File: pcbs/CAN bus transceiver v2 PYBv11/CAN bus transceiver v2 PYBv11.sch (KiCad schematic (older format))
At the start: 5 parts, among them P1 CONN_01X16, P2 CONN_01X02, P3 CONN_01X16, U1 TCAN337GDR, U2 TCAN337GDR

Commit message: working on CAN bus transceiver v2 PYBv11 shield
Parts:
- removed P1, P3: CONN_01X16, Pin_Headers:Pin_Header_Straight_1x16, symbol CONN_01X16
- added P1, P3: CONN_01X06, Pin_Headers:Pin_Header_Straight_1x06, symbol CONN_01X06
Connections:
- net +3V3: now also P3.2 (P2)
- net GND: now also P3.3 (P3)
- net at U1.1 (TX): now also P1.4 (P4)
- net at U1.4 (RX): now also P1.3 (P3)
- net at U1.5 (FAULT): now also P3.5 (P5)
- net at U1.8 (S): now also P1.1 (P1)
- net at U2.1 (TX): now also P1.6 (P6)
- net at U2.4 (RX): now also P1.5 (P5)
- net at U2.5 (FAULT): now also P3.6 (P6)
- net at U2.8 (S): now also P1.2 (P2)
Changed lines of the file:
@@
 LIBS:valves
 LIBS:can
+LIBS:CAN bus transceiver v2 PYBv11-cache
 EELAYER 25 0
 EELAYER END
@@
 	1    0    0    -1
 $EndComp
-$Comp
-L CONN_01X16 P1
-U 1 1 58129A6E
-P 1500 2250
-F 0 "P1" H 1500 3100 50  0000 C CNN
-F 1 "CONN_01X16" V 1600 2250 50  0000 C CNN
-F 2 "Pin_Headers:Pin_Header_Straight_1x16" H 1500 2250 50  0001 C CNN
-F 3 "" H 1500 2250 50  0000 C CNN
-	1    1500 2250
-	-1   0    0    -1
-$EndComp
-$Comp
-L CONN_01X16 P3
-U 1 1 58129D53
-P 4525 2250
-F 0 "P3" H 4525 3100 50  0000 C CNN
-F 1 "CONN_01X16" V 4625 2250 50  0000 C CNN
-F 2 "Pin_Headers:Pin_Header_Straight_1x16" H 4525 2250 50  0001 C CNN
-F 3 "" H 4525 2250 50  0000 C CNN
-	1    4525 2250
-	1    0    0    -1
-$EndComp
 Text Notes 1000 1700 0    60   ~ 0
 CAN1 RX
@@
 $EndComp
 Wire Wire Line
-	2150 1175 2150 2900
-Wire Wire Line
-	2150 2900 1700 2900
-Wire Wire Line
 	2650 1775 2150 1775
 Connection ~ 2150 1775
 Wire Wire Line
-	2650 2650 2150 2650
-Connection ~ 2150 2650
-Wire Wire Line
 	2650 1700 2250 1700
 Wire Wire Line
@@
 	2650 2575 2250 2575
 Connection ~ 2250 2575
-Wire Wire Line
-	1700 2800 2250 2800
-Connection ~ 2250 2800
 Wire Wire Line
 	2650 1625 2050 1625
@@
 Wire Wire Line
 	1925 1600 1700 1600
+Wire Wire Line
+	2650 2650 2150 2650
+Wire Wire Line
+	2150 2650 2150 1175
+$Comp
+L CONN_01X06 P1
+U 1 1 58144AB1
+P 1500 1750
+F 0 "P1" H 1500 2100 50  0000 C CNN
+F 1 "CONN_01X06" V 1600 1750 50  0000 C CNN
+F 2 "Pin_Headers:Pin_Header_Straight_1x06" H 1500 1750 50  0001 C CNN
+F 3 "" H 1500 1750 50  0000 C CNN
+	1    1500 1750
+	-1   0    0    -1
+$EndComp
+$Comp
+L CONN_01X06 P3
+U 1 1 58144C08
+P 4525 1750
+F 0 "P3" H 4525 2100 50  0000 C CNN
+F 1 "CONN_01X06" V 4625 1750 50  0000 C CNN
+F 2 "Pin_Headers:Pin_Header_Straight_1x06" H 4525 1750 50  0001 C CNN
+F 3 "" H 4525 1750 50  0000 C CNN
+	1    4525 1750
+	1    0    0    -1
+$EndComp
 $EndSCHEMATC

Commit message: working on CAN bus transceiver v2 PYBv11 shield
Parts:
- added P2: CONN_01X02, Connectors_JST:JST_XH_S02B-XH-A_02x2.50mm_Angled, symbol CONN_01X02
- renumbered P2 to P3, P3 to P4
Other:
- note added: "CAN1 FAULT"
- note added: "CAN1 S"
- note added: "CAN2 FAULT"
- note added: "CAN2 S"
- moved on the sheet: P1, P3, P4, U1, U2
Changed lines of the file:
@@
 L TCAN337GDR U1
 U 1 1 581297E0
-P 3075 1725
-F 0 "U1" H 3075 1450 60  0000 C CNN
-F 1 "TCAN337GDR" H 3075 1975 60  0000 C CNN
-F 2 "Housings_SOIC:SOIC-8_3.9x4.9mm_Pitch1.27mm" H 3000 1550 60  0001 C CNN
-F 3 "" H 3000 1550 60  0000 C CNN
-	1    3075 1725
+P 3675 2475
+F 0 "U1" H 3675 2200 60  0000 C CNN
+F 1 "TCAN337GDR" H 3675 2725 60  0000 C CNN
+F 2 "Housings_SOIC:SOIC-8_3.9x4.9mm_Pitch1.27mm" H 3600 2300 60  0001 C CNN
+F 3 "" H 3600 2300 60  0000 C CNN
+	1    3675 2475
 	1    0    0    -1
 $EndComp
@@
 L TCAN337GDR U2
 U 1 1 58129949
-P 3075 2600
-F 0 "U2" H 3075 2325 60  0000 C CNN
-F 1 "TCAN337GDR" H 3075 2850 60  0000 C CNN
-F 2 "Housings_SOIC:SOIC-8_3.9x4.9mm_Pitch1.27mm" H 3000 2425 60  0001 C CNN
-F 3 "" H 3000 2425 60  0000 C CNN
-	1    3075 2600
-	1    0    0    -1
-$EndComp
-Text Notes 1000 1700 0    60   ~ 0
+P 3675 3350
+F 0 "U2" H 3675 3075 60  0000 C CNN
+F 1 "TCAN337GDR" H 3675 3600 60  0000 C CNN
+F 2 "Housings_SOIC:SOIC-8_3.9x4.9mm_Pitch1.27mm" H 3600 3175 60  0001 C CNN
+F 3 "" H 3600 3175 60  0000 C CNN
+	1    3675 3350
+	1    0    0    -1
+$EndComp
+Text Notes 1600 2275 0    60   ~ 0
 CAN1 RX
-Text Notes 1000 1800 0    60   ~ 0
+Text Notes 1600 2375 0    60   ~ 0
 CAN1 TX
-Text Notes 1000 1900 0    60   ~ 0
+Text Notes 1600 2575 0    60   ~ 0
 CAN2 RX
-Text Notes 1000 2000 0    60   ~ 0
+Text Notes 1600 2675 0    60   ~ 0
 CAN2 TX
-Text Notes 1225 2825 0    60   ~ 0
-GND
-Text Notes 1225 2925 0    60   ~ 0
-3V3
 $Comp
 L GND #PWR01
 U 1 1 58129EE2
-P 2250 3350
-F 0 "#PWR01" H 2250 3100 50  0001 C CNN
-F 1 "GND" H 2250 3200 50  0000 C CNN
-F 2 "" H 2250 3350 50  0000 C CNN
-F 3 "" H 2250 3350 50  0000 C CNN
-	1    2250 3350
+P 2850 4100
+F 0 "#PWR01" H 2850 3850 50  0001 C CNN
+F 1 "GND" H 2850 3950 50  0000 C CNN
+F 2 "" H 2850 4100 50  0000 C CNN
+F 3 "" H 2850 4100 50  0000 C CNN
+	1    2850 4100
 	1    0    0    -1
 $EndComp
@@
 L +3.3V #PWR02
 U 1 1 58129EFE
-P 2150 1175
-F 0 "#PWR02" H 2150 1025 50  0001 C CNN
-F 1 "+3.3V" H 2150 1315 50  0000 C CNN
-F 2 "" H 2150 1175 50  0000 C CNN
-F 3 "" H 2150 1175 50  0000 C CNN
-	1    2150 1175
-	1    0    0    -1
-$EndComp
-Wire Wire Line
-	2650 1775 2150 1775
-Connection ~ 2150 1775
-Wire Wire Line
-	2650 1700 2250 1700
-Wire Wire Line
-	2250 1700 2250 3350
-Wire Wire Line
-	2650 2575 2250 2575
-Connection ~ 2250 2575
-Wire Wire Line
-	2650 1625 2050 1625
-Wire Wire Line
-	2050 1625 2050 1800
-Wire Wire Line
-	2050 1800 1700 1800
-Wire Wire Line
-	2650 1850 2000 1850
-Wire Wire Line
-	2000 1850 2000 1700
-Wire Wire Line
-	2000 1700 1700 1700
-Wire Wire Line
-	2650 2725 1900 2725
-Wire Wire Line
-	1900 2725 1900 1900
-Wire Wire Line
-	1900 1900 1700 1900
-Wire Wire Line
-	2650 2500 1800 2500
-Wire Wire Line
-	1800 2500 1800 2000
-Wire Wire Line
-	1800 2000 1700 2000
-Text Notes 4625 1600 0    60   ~ 0
+P 2750 725
+F 0 "#PWR02" H 2750 575 50  0001 C CNN
+F 1 "+3.3V" H 2750 865 50  0000 C CNN
+F 2 "" H 2750 725 50  0000 C CNN
+F 3 "" H 2750 725 50  0000 C CNN
+	1    2750 725
+	1    0    0    -1
+$EndComp
+Wire Wire Line
+	3250 2525 2750 2525
+Connection ~ 2750 2525
+Wire Wire Line
+	3250 2450 2850 2450
+Wire Wire Line
+	3250 3325 2850 3325
+Connection ~ 2850 3325
+Wire Wire Line
+	3250 2375 2650 2375
+Wire Wire Line
+	2650 2375 2650 2550
+Wire Wire Line
+	2650 2550 2300 2550
+Wire Wire Line
+	3250 2600 2600 2600
+Wire Wire Line
+	2600 2600 2600 2450
+Wire Wire Line
+	2600 2450 2300 2450
+Wire Wire Line
+	3250 3475 2500 3475
+Wire Wire Line
+	2500 3475 2500 2650
+Wire Wire Line
+	2500 2650 2300 2650
+Wire Wire Line
+	3250 3250 2400 3250
+Wire Wire Line
+	2400 3250 2400 2750
+Wire Wire Line
+	2400 2750 2300 2750
+Text Notes 5225 2350 0    60   ~ 0
 3V3
-Text Notes 4625 1700 0    60   ~ 0
+Text Notes 5225 2450 0    60   ~ 0
 GND
 Wire Wire Line
-	4325 1700 4175 1700
-Wire Wire Line
-	4175 1700 4175 3100
-Wire Wire Line
-	4175 3100 2250 3100
-Connection ~ 2250 3100
-Wire Wire Line
-	4325 1600 4175 1600
-Wire Wire Line
-	4175 1600 4175 1250
-Wire Wire Line
-	4175 1250 2150 1250
-Connection ~ 2150 1250
-$Comp
-L CONN_01X02 P2
+	4925 2450 4775 2450
+Wire Wire Line
+	4775 2450 4775 3850
+Wire Wire Line
+	4775 3850 2850 3850
+Connection ~ 2850 3850
+Wire Wire Line
+	4925 2350 4775 2350
+Wire Wire Line
+	4775 2350 4775 2000
+Wire Wire Line
+	4775 2000 2750 2000
+Connection ~ 2750 2000
+$Comp
+L CONN_01X02 P3
 U 1 1 5812A45B
-P 4525 975
-F 0 "P2" H 4525 1125 50  0000 C CNN
-F 1 "CONN_01X02" V 4625 975 50  0000 C CNN
-F 2 "Connectors_JST:JST_XH_S02B-XH-A_02x2.50mm_Angled" H 4525 975 50  0001 C CNN
-F 3 "" H 4525 975 50  0000 C CNN
-	1    4525 975
-	1    0    0    -1
-$EndComp
-Text Notes 4700 925  0    60   ~ 0
+P 5125 1725
+F 0 "P3" H 5125 1875 50  0000 C CNN
+F 1 "CONN_01X02" V 5225 1725 50  0000 C CNN
+F 2 "Connectors_JST:JST_XH_S02B-XH-A_02x2.50mm_Angled" H 5125 1725 50  0001 C CNN
+F 3 "" H 5125 1725 50  0000 C CNN
+	1    5125 1725
+	1    0    0    -1
+$EndComp
+Text Notes 5300 1675 0    60   ~ 0
 CANH
-Text Notes 4700 1050 0    60   ~ 0
+Text Notes 5300 1800 0    60   ~ 0
 CANL
 Wire Wire Line
-	3475 2575 4000 2575
-Wire Wire Line
-	4000 2575 4000 925
-Wire Wire Line
-	4000 925  4325 925
-Wire Wire Line
-	3475 1700 4000 1700
-Connection ~ 4000 1700
-Wire Wire Line
-	3475 2650 4100 2650
-Wire Wire Line
-	4100 2650 4100 1025
-Wire Wire Line
-	4100 1025 4325 1025
-Wire Wire Line
-	3475 1775 4100 1775
-Connection ~ 4100 1775
-Wire Wire Line
-	3475 1850 3475 1900
-Wire Wire Line
-	3475 1900 4325 1900
-Wire Wire Line
-	3475 2725 3950 2725
-Wire Wire Line
-	3950 2725 3950 2000
-Wire Wire Line
-	3950 2000 4325 2000
-Wire Wire Line
-	3475 1625 3550 1625
-Wire Wire Line
-	3550 1625 3550 1300
-Wire Wire Line
-	3550 1300 1825 1300
-Wire Wire Line
-	1825 1300 1825 1500
-Wire Wire Line
-	1825 1500 1700 1500
-Wire Wire Line
-	3475 2500 3650 2500
-Wire Wire Line
-	3650 2500 3650 1400
-Wire Wire Line
-	3650 1400 1925 1400
-Wire Wire Line
-	1925 1400 1925 1600
-Wire Wire Line
-	1925 1600 1700 1600
-Wire Wire Line
-	2650 2650 2150 2650
-Wire Wire Line
-	2150 2650 2150 1175
+	4075 3325 4600 3325
+Wire Wire Line
+	4600 3325 4600 1675
+Wire Wire Line
+	4600 1675 4925 1675
+Wire Wire Line
+	4075 2450 4600 2450
+Connection ~ 4600 2450
+Wire Wire Line
+	4075 3400 4700 3400
+Wire Wire Line
+	4700 3400 4700 1775
+Wire Wire Line
+	4700 1775 4925 1775
+Wire Wire Line
+	4075 2525 4700 2525
+Connection ~ 4700 2525
+Wire Wire Line
+	4075 2600 4075 2650
+Wire Wire Line
+	4075 2650 4925 2650
+Wire Wire Line
+	4075 3475 4550 3475
+Wire Wire Line
+	4550 3475 4550 2750
+Wire Wire Line
+	4550 2750 4925 2750
+Wire Wire Line
+	4075 2375 4150 2375
+Wire Wire Line
+	4150 2375 4150 2050
+Wire Wire Line
+	4150 2050 2425 2050
+Wire Wire Line
+	2425 2050 2425 2250
+Wire Wire Line
+	2425 2250 2300 2250
+Wire Wire Line
+	4075 3250 4250 3250
+Wire Wire Line
+	4250 3250 4250 2150
+Wire Wire Line
+	4250 2150 2525 2150
+Wire Wire Line
+	2525 2150 2525 2350
+Wire Wire Line
+	2525 2350 2300 2350
+Wire Wire Line
+	2750 3400 3250 3400
+Wire Wire Line
+	2750 725  2750 3400
 $Comp
 L CONN_01X06 P1
 U 1 1 58144AB1
-P 1500 1750
-F 0 "P1" H 1500 2100 50  0000 C CNN
-F 1 "CONN_01X06" V 1600 1750 50  0000 C CNN
-F 2 "Pin_Headers:Pin_Header_Straight_1x06" H 1500 1750 50  0001 C CNN
-F 3 "" H 1500 1750 50  0000 C CNN
-	1    1500 1750
+P 2100 2500
+F 0 "P1" H 2100 2850 50  0000 C CNN
+F 1 "CONN_01X06" V 2200 2500 50  0000 C CNN
+F 2 "Pin_Headers:Pin_Header_Straight_1x06" H 2100 2500 50  0001 C CNN
+F 3 "" H 2100 2500 50  0000 C CNN
+	1    2100 2500
 	-1   0    0    -1
 $EndComp
 $Comp
-L CONN_01X06 P3
+L CONN_01X06 P4
 U 1 1 58144C08
-P 4525 1750
-F 0 "P3" H 4525 2100 50  0000 C CNN
-F 1 "CONN_01X06" V 4625 1750 50  0000 C CNN
-F 2 "Pin_Headers:Pin_Header_Straight_1x06" H 4525 1750 50  0001 C CNN
-F 3 "" H 4525 1750 50  0000 C CNN
-	1    4525 1750
-	1    0    0    -1
-$EndComp
+P 5125 2500
+F 0 "P4" H 5125 2850 50  0000 C CNN
+F 1 "CONN_01X06" V 5225 2500 50  0000 C CNN
+F 2 "Pin_Headers:Pin_Header_Straight_1x06" H 5125 2500 50  0001 C CNN
+F 3 "" H 5125 2500 50  0000 C CNN
+	1    5125 2500
+	1    0    0    -1
+$EndComp
+$Comp
+L CONN_01X02 P2
+U 1 1 5816EBA7
+P 5125 1100
+F 0 "P2" H 5125 1250 50  0000 C CNN
+F 1 "CONN_01X02" V 5225 1100 50  0000 C CNN
+F 2 "Connectors_JST:JST_XH_S02B-XH-A_02x2.50mm_Angled" H 5125 1100 50  0001 C CNN
+F 3 "" H 5125 1100 50  0000 C CNN
+	1    5125 1100
+	1    0    0    -1
+$EndComp
+Text Notes 5225 2650 0    60   ~ 0
+CAN1 FAULT
+Text Notes 5225 2750 0    60   ~ 0
+CAN2 FAULT
+Text Notes 1600 2775 0    60   ~ 0
+CAN2 S
+Text Notes 1600 2475 0    60   ~ 0
+CAN1 S
+Wire Wire Line
+	2850 2450 2850 4100
 $EndSCHEMATC

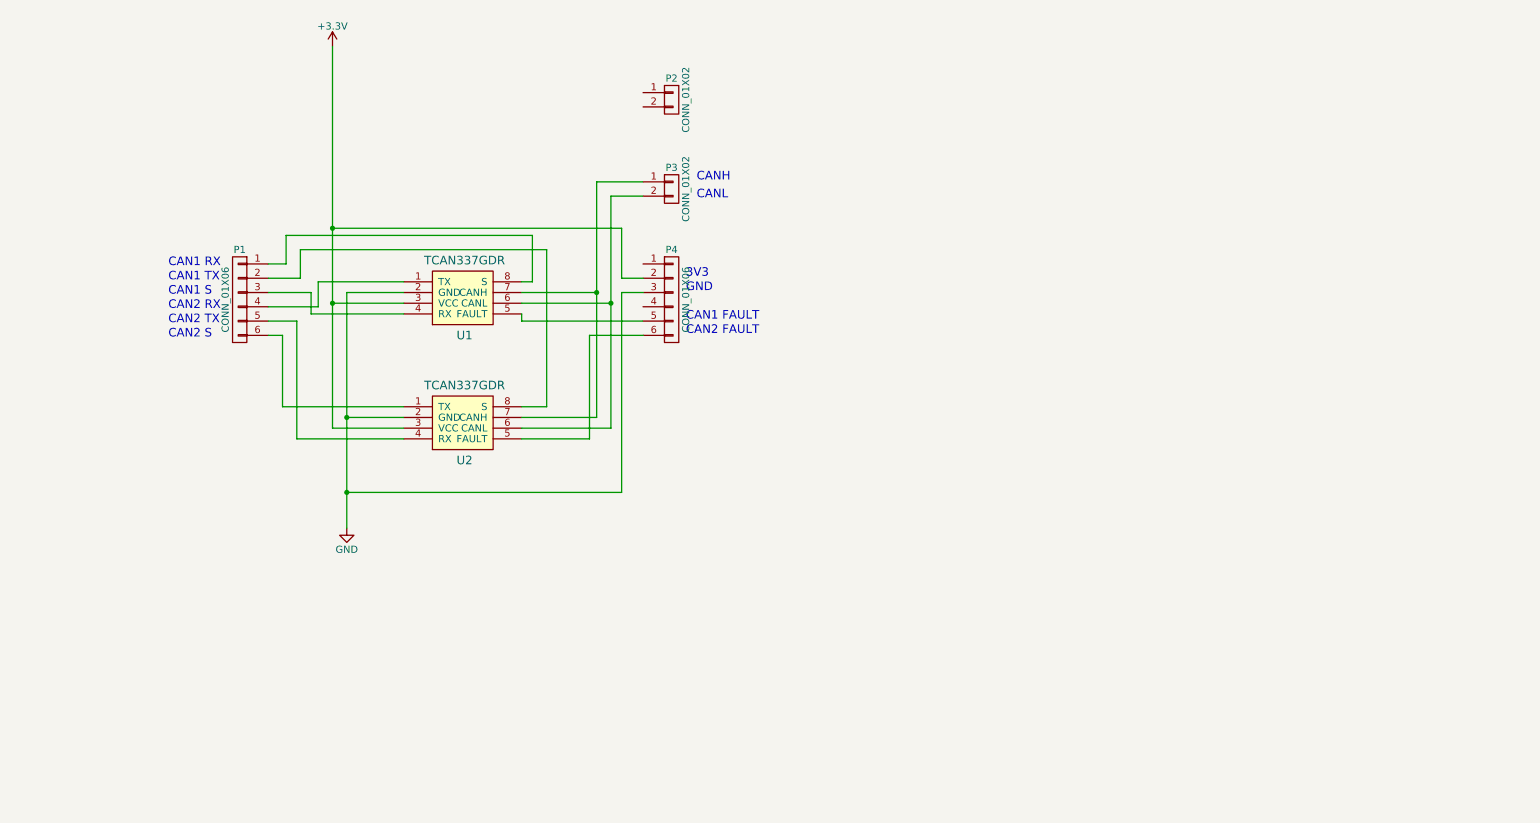
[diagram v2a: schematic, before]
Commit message: working on CAN bus transceiver v2 PYBv11 shield
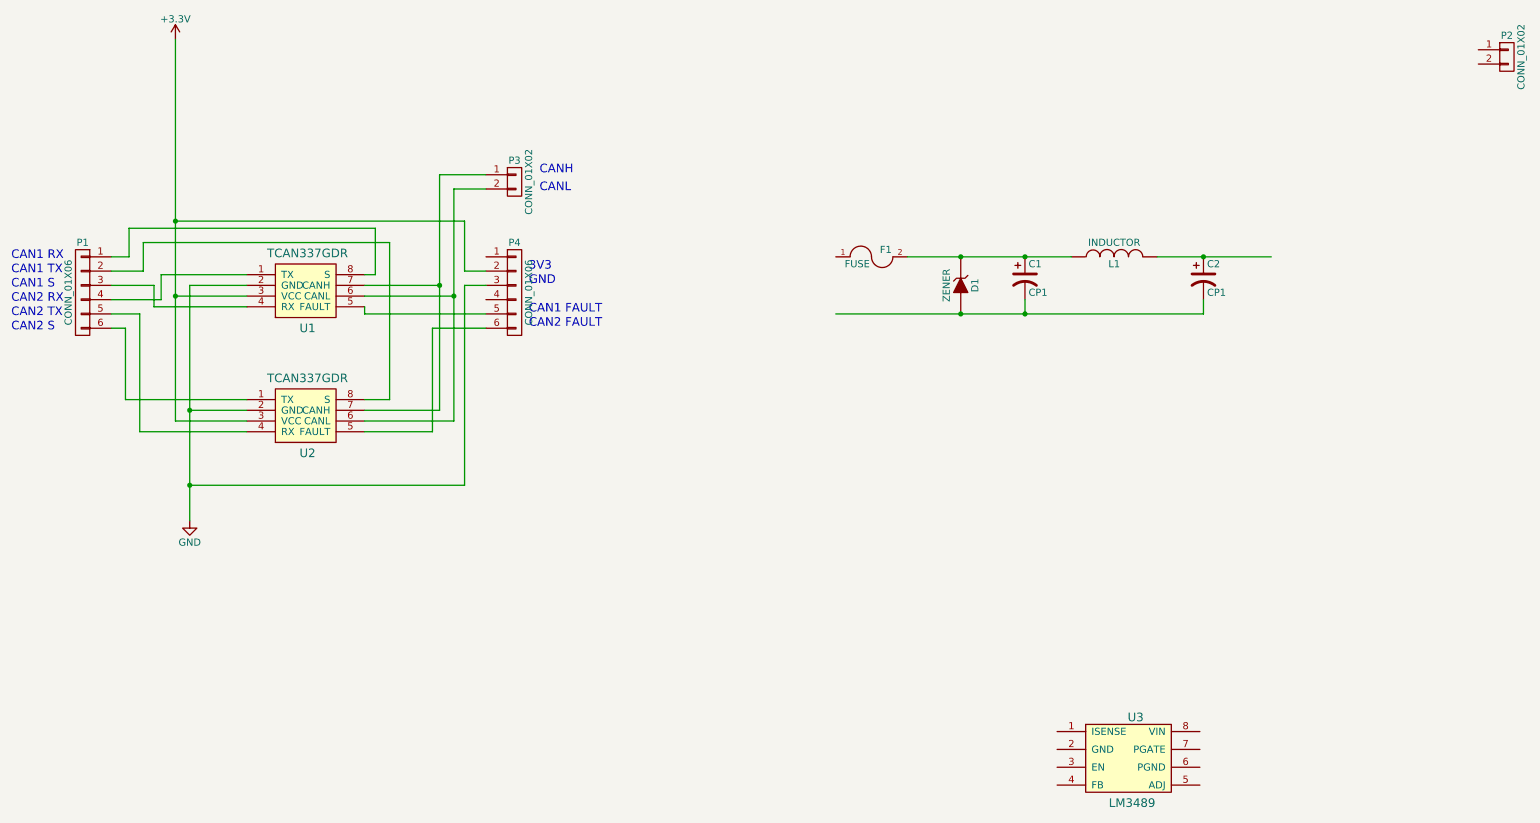
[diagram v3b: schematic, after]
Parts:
- added C1, C2: CP1, Capacitors_ThroughHole:C_Radial_D8_L11.5_P3.5, symbol CP1
- added D1: ZENER, Diodes_SMD:SMB_Handsoldering, symbol ZENER
- added F1: FUSE, Resistors_SMD:R_0805_HandSoldering, symbol FUSE
- added L1: INDUCTOR, Inductors:Inductor_Taiyo-Yuden_NR-80xx_HandSoldering, symbol INDUCTOR
- added U3: LM3489, symbol LM3489
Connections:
- wire segments 47 -> 52
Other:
- moved on the sheet: P1, P2, P3, P4, U1, U2

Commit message: doc: added docs for Pioneer AVH-X7500BT and Texas Instruments LM3489
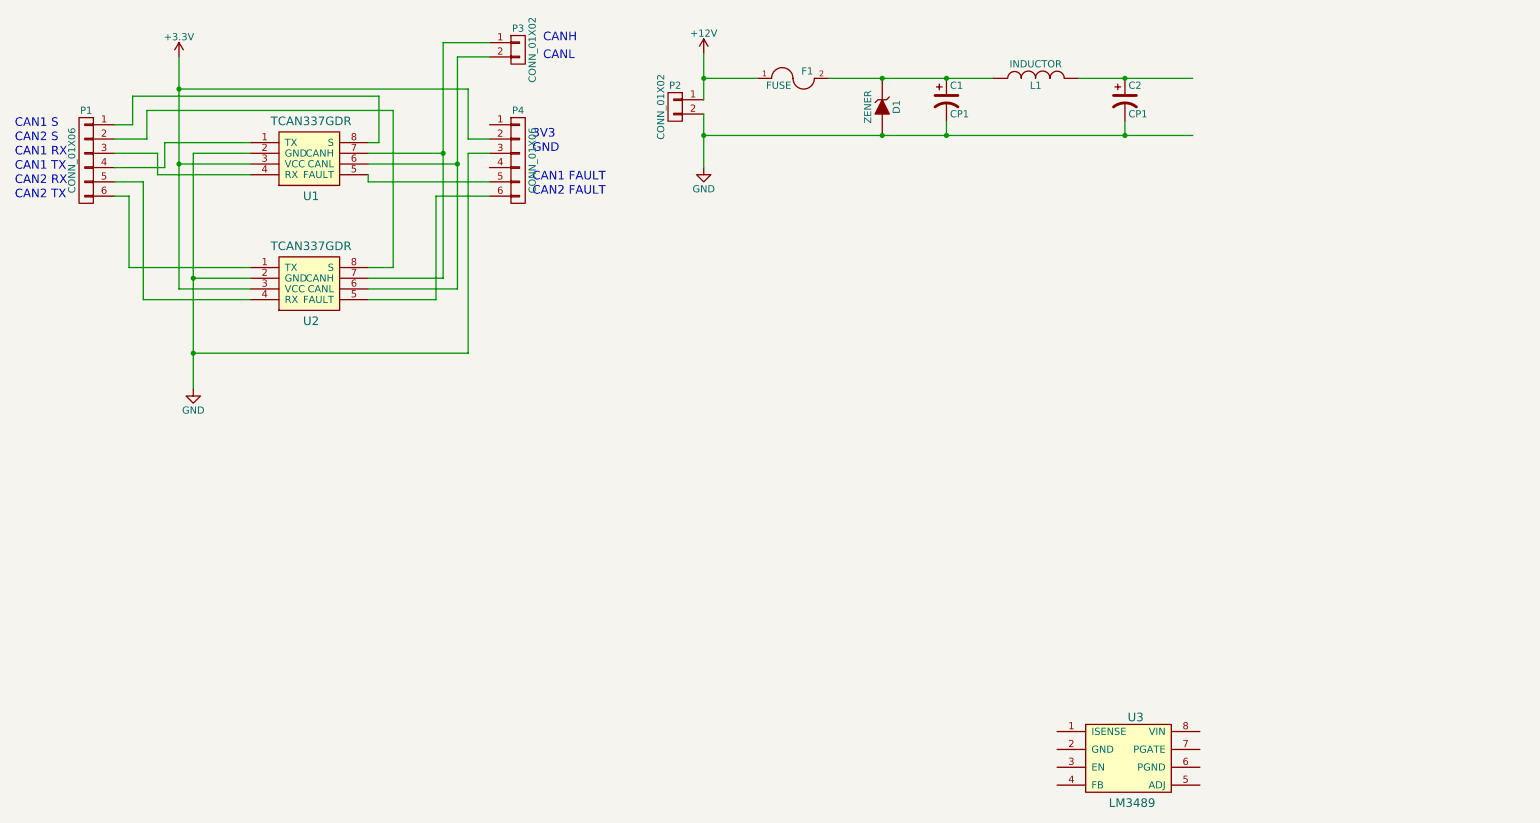
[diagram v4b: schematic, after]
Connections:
- net labels added: +12V
- wire segments 52 -> 55
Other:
- moved on the sheet: C1, C2, D1, F1, L1, P1, P2, P3, P4, U1, U2

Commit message: can: added components for LM3489 wiring
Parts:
- removed C2: CP1, Capacitors_ThroughHole:C_Radial_D8_L11.5_P3.5, symbol CP1
- removed F1: FUSE, Resistors_SMD:R_0805_HandSoldering, symbol FUSE
- removed P2: CONN_01X02, Connectors_JST:JST_XH_S02B-XH-A_02x2.50mm_Angled, symbol CONN_01X02
- added C2, C3, C4: C, Capacitors_SMD:C_0805, symbol C
- added C5: CP1, Capacitors_ThroughHole:C_Radial_D8_L11.5_P3.5, symbol CP1
- added D2: D_Schottky, Diodes_ThroughHole:Diode_DO-35_SOD27_Horizontal_RM10, symbol D_Schottky
- added P4: CONN_01X02, Connectors_JST:JST_XH_S02B-XH-A_02x2.50mm_Angled, symbol CONN_01X02
- added Q1: Q_PMOS_SGD, TO_SOT_Packages_THT:SOT126_SOT32_Housing_Vertical, symbol Q_PMOS_SGD
- added R1, R2, R3, R4: R, Resistors_SMD:R_0805, symbol R
- U3: footprint (none) -> Housings_SSOP:TSSOP-8_4.4x3mm_Pitch0.65mm
- renumbered P3 to P2, P4 to P3
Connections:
- net labels added: +5V
- wire segments 55 -> 89
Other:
- moved on the sheet: D1, U3
